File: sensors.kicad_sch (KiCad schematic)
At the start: 39 parts, among them J1 Amphenol_901-144, J2 Amphenol_901-144, Q1 BSS138DWQ-7, Q2 MBT2222ADW1T1, Q3 BSS138DWQ-7, Q4 MBT2222ADW1T1, Q5 MMDT2907, Q8 IRLML2803, Q9 NDS8434, U2 BMM150, U3 BMI270, U4 S1216V8, U5 EP2W+

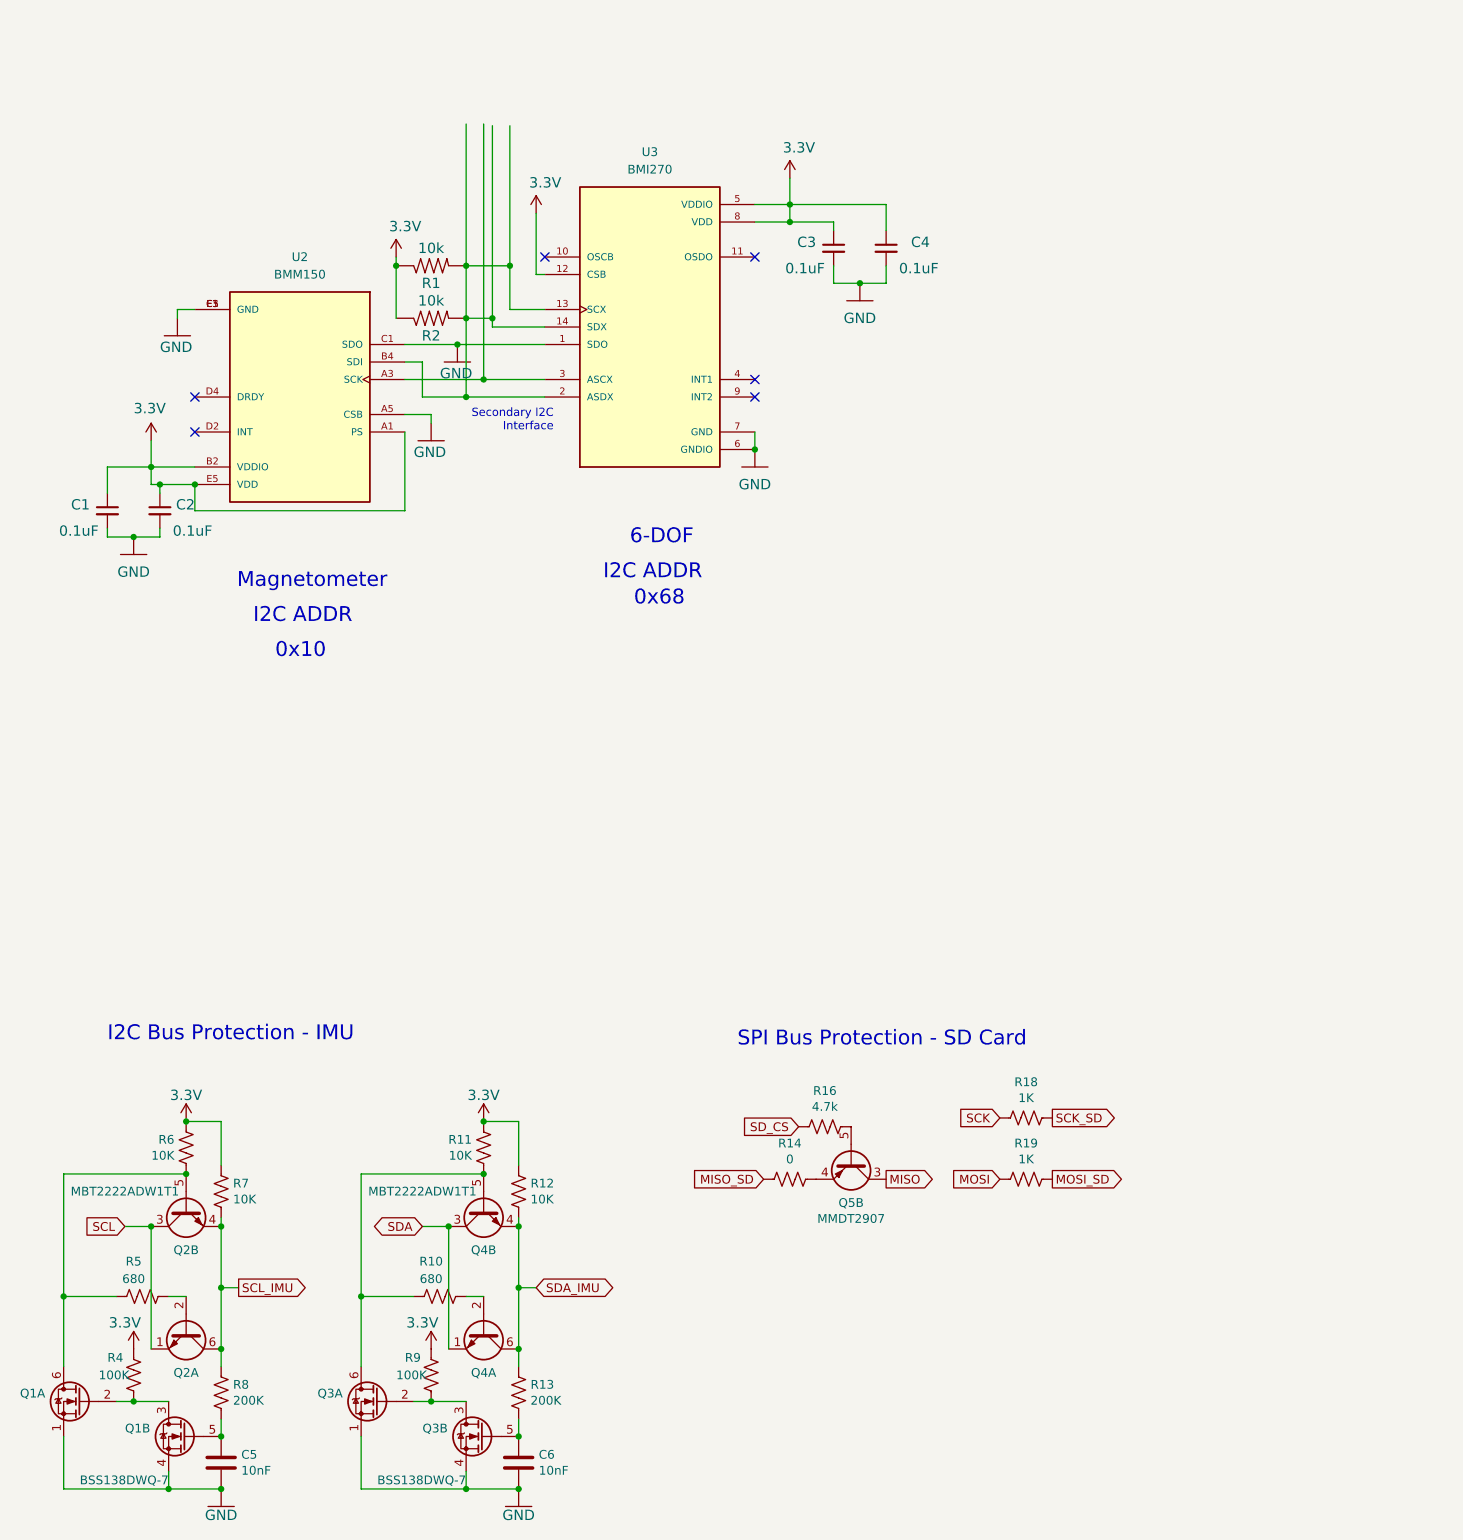
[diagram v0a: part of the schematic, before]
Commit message: update schematic
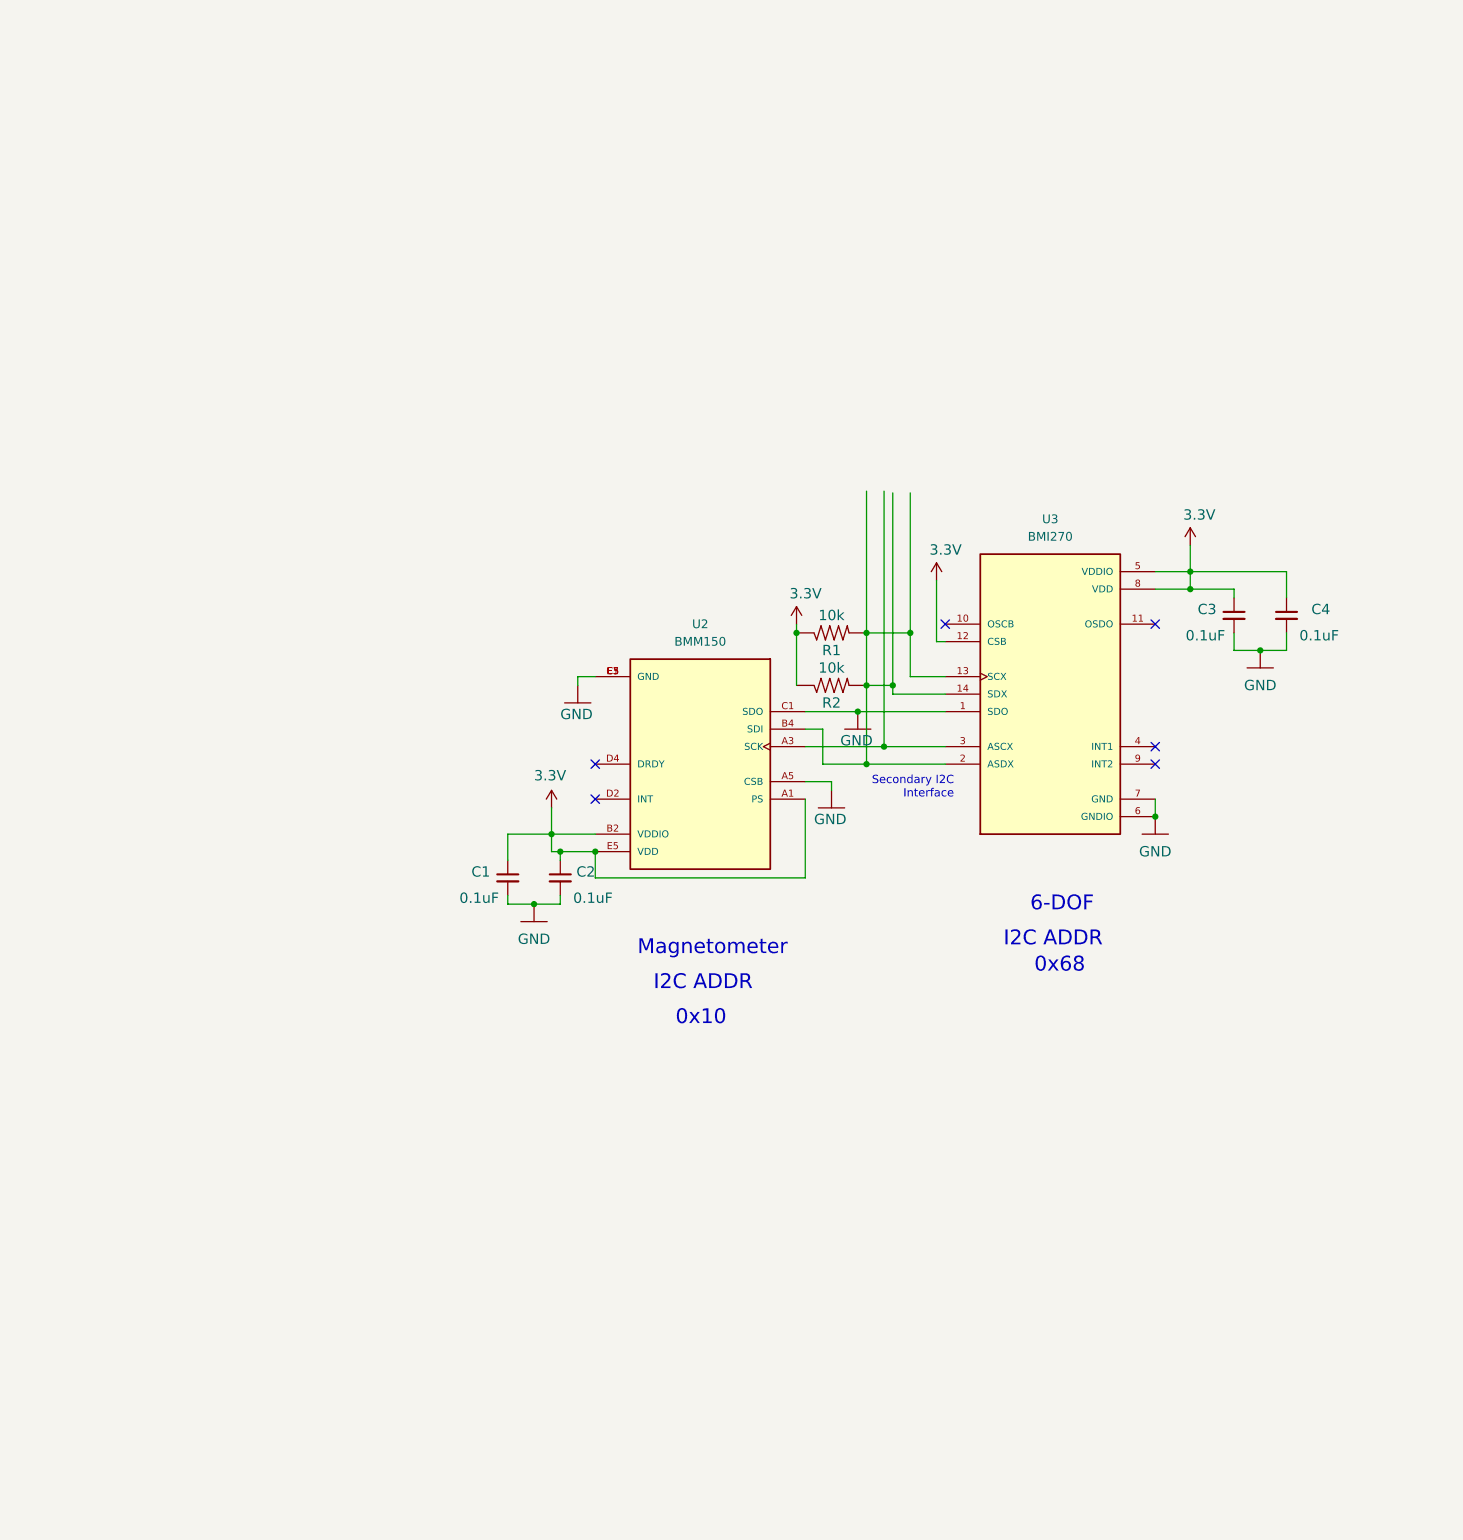
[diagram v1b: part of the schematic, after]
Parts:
- removed C5, C6: 10nF, Capacitor_SMD:C_0603_1608Metric, symbol Device:C
- removed Q1, Q3: BSS138DWQ-7, mainboard:BSS138DWQ-7, symbol mainboard:BSS138DWQ-7
- removed Q2, Q4: MBT2222ADW1T1, Package_TO_SOT_SMD:SOT-363_SC-70-6, symbol Transistor_BJT:MBT2222ADW1T1
- removed Q5: MMDT2907, Package_TO_SOT_SMD:SOT-363_SC-70-6, symbol mainboard:MMDT2907
- removed R10, R5: 680, Resistor_SMD:R_0603_1608Metric, symbol Device:R_US
- removed R11, R12, R6, R7: 10K, Resistor_SMD:R_0603_1608Metric, symbol Device:R_US
- removed R13, R8: 200K, Resistor_SMD:R_0603_1608Metric, symbol Device:R_US
- removed R14: 0, Resistor_SMD:R_0603_1608Metric, symbol Device:R_US
- removed R16: 4.7k, Resistor_SMD:R_0603_1608Metric, symbol Device:R_US
- removed R18, R19: 1K, Resistor_SMD:R_0603_1608Metric, symbol Device:R_US
- removed R4, R9: 100K, Resistor_SMD:R_0603_1608Metric, symbol Device:R_US
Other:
- note removed: "I2C Bus Protection - IMU"
- note removed: "SPI Bus Protection - SD Card"
- moved on the sheet: C1, C2, C3, C4, R1, R2, U2, U3

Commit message: hmm
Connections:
- net VBATT is gone; now on net GPS_PWR_IN: U4.22 (V_BCKP)
- net 3.3V: no longer Q9.1 (Source), Q9.2 (Source), Q9.3 (Source), R33.1
- net IMU_SCL: now reaches R1.2, R2.2, U2.B4 (SDI), U3.13 (SCX), U3.14 (SDX), U3.2 (ASDX)
- new net 3V3_IN: Q9.1 (Source), Q9.2 (Source), Q9.3 (Source), R33.1
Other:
- note added: "GPS_PWR_IN is 3v3 but from the PyCubed Mainboard regulator. This way, the GPS stays on when if the ADCS board resets (but not when the mainboard 3v3 regulator resets)."
- note added: "I originally made this circuit based on datasheet of the BMI270, and then handed off to evelyn. Nobody has tested the code with the secondary i2c interface, idk what the benefit of doing this would even be (other than just increasing available I2C address space). I don't think the address of the magnetometer is actuall 0x10"
- note added: "Per datasheet, V_BCKP current draw is 15 μA"
- note removed: "Per datasheet, V_BCKP current draw is 15 μA TODO do we want a seperate, always on 3v3 regulator here?"
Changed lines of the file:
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@@
   (junction (at 160.9852 108.1532) (diameter 0) (color 0 0 0 0)
-  )
-  (junction (at 157.1752 124.6632) (diameter 0) (color 0 0 0 0)
   )
   (junction (at 106.3752 147.5232) (diameter 0) (color 0 0 0 0)
@@
     (stroke (width 0) (type default))
   )
-  (wire (pts (xy 157.1752 124.6632) (xy 166.0652 124.6632))
+  (wire (pts (xy 145.7452 124.6632) (xy 166.0652 124.6632))
     (stroke (width 0) (type default))
   )
@@
     (stroke (width 0) (type default))
   )
-  (wire (pts (xy 157.1752 124.6632) (xy 157.1752 87.5792))
-    (stroke (width 0) (type default))
-  )
   (wire (pts (xy 158.4452 117.0432) (xy 158.4452 115.7732))
     (stroke (width 0) (type default))
   )
-  (wire (pts (xy 145.7452 124.6632) (xy 157.1752 124.6632))
-    (stroke (width 0) (type default))
-  )
   (wire (pts (xy 145.7452 129.7432) (xy 149.5552 129.7432))
     (stroke (width 0) (type default))
@@
     (stroke (width 0) (type default))
   )
-  (wire (pts (xy 158.4452 115.7732) (xy 158.4452 87.8332))
+  (wire (pts (xy 159.512 115.7732) (xy 159.512 84.0232))
     (stroke (width 0) (type default))
   )
@@
   )
   (wire (pts (xy 353.06 160.02) (xy 337.82 160.02))
+    (stroke (width 0) (type default))
+  )
+  (wire (pts (xy 159.512 115.7732) (xy 158.4452 115.7732))
     (stroke (width 0) (type default))
   )
@@
     (effects (font (size 2.159 2.159)) (justify left bottom))
   )
-  (text "Per datasheet, V_BCKP\ncurrent draw is 15 μA\n\nTODO do we want a\nseperate, always on \n3v3 regulator here?"
-    (at 356.87 88.9 0)
+  (text "Per datasheet, V_BCKP\ncurrent draw is 15 μA" (at 353.2632 88.9508 0)
     (effects (font (size 1.27 1.27)) (justify left bottom))
   )
-  (text "0x68" (at 186.3852 157.6832 0)
+  (text "I originally made this circuit based on datasheet of the BMI270, and \nthen handed off to evelyn. Nobody has tested the code with the secondary \ni2c interface, idk what the benefit of doing this would even be \n(other than just increasing available I2C address space).\n\nI don't think the address of the magnetometer is actuall 0x10\n"
+    (at 124.8664 182.4228 0)
+    (effects (font (size 1.2 1.2)) (justify left bottom))
+  )
+  (text "0x68" (at 185.0644 158.1404 0)
     (effects (font (size 2.159 2.159)) (justify right bottom))
   )
@@
     (effects (font (size 1.2 1.2)) (justify right bottom))
   )
-  (text "I2C ADDR" (at 188.9252 153.8732 0)
+  (text "I2C ADDR" (at 190.3984 153.8224 0)
     (effects (font (size 2.159 2.159)) (justify right bottom))
   )
@@
     (effects (font (size 2.159 2.159)) (justify right bottom))
   )
+  (text "GPS_PWR_IN is 3v3 but from the \nPyCubed Mainboard regulator. \nThis way, the GPS stays on when \nif the ADCS board resets (but not\nwhen the mainboard 3v3 regulator\nresets).\n"
+    (at 374.5484 103.4796 0)
+    (effects (font (size 1.27 1.27) (color 249 0 0 1)) (justify left bottom))
+  )
   (text "0x10\n" (at 134.3152 165.3032 0)
     (effects (font (size 2.159 2.159)) (justify right bottom))
@@
     (effects (font (size 1.27 1.27)) (justify left bottom))
   )
-  (global_label "GND" (shape bidirectional) (at 379.73 134.62 180) (fields_autoplaced)
-    (effects (font (size 0.254 0.254)) (justify right))
-    (property "Intersheetrefs" "${INTERSHEET_REFS}" (at 378.2988 134.62 0)
-      (effects (font (size 1.27 1.27)) (justify right) hide)
+  (global_label "IMU_SDA" (shape input) (at 159.512 84.0232 0) (fields_autoplaced)
+    (effects (font (size 1.27 1.27)) (justify left))
+    (property "Intersheetrefs" "${INTERSHEET_REFS}" (at 170.4196 84.0232 0)
+      (effects (font (size 1.27 1.27)) (justify left) hide)
     )
   )
@@
     )
   )
+  (global_label "3V3_IN" (shape bidirectional) (at 320.04 80.01 180) (fields_autoplaced)
+    (effects (font (size 1.27 1.27)) (justify right))
+    (property "Intersheetrefs" "${INTERSHEET_REFS}" (at 309.533 80.01 0)
+      (effects (font (size 1.27 1.27)) (justify right) hide)
+    )
+  )
   (global_label "GPS_PWR_IN" (shape bidirectional) (at 367.03 168.91 0) (fields_autoplaced)
     (effects (font (size 1.27 1.27)) (justify left))
@@
     )
   )
-  (global_label "GND" (shape bidirectional) (at 302.26 185.42 180) (fields_autoplaced)
-    (effects (font (size 0.254 0.254)) (justify right))
-    (property "Intersheetrefs" "${INTERSHEET_REFS}" (at 300.8288 185.42 0)
-      (effects (font (size 1.27 1.27)) (justify right) hide)
-    )
-  )
-  (global_label "VBATT" (shape bidirectional) (at 299.72 180.34 180) (fields_autoplaced)
-    (effects (font (size 1.27 1.27)) (justify right))
-    (property "Intersheetrefs" "${INTERSHEET_REFS}" (at 290.2411 180.34 0)
-      (effects (font (size 1.27 1.27)) (justify right) hide)
-    )
-  )
   (global_label "GPS_PWR_IN" (shape bidirectional) (at 351.79 92.71 0) (fields_autoplaced)
     (effects (font (size 1.27 1.27)) (justify left))
@@
     )
   )
-  (global_label "GND" (shape bidirectional) (at 337.82 154.94 180) (fields_autoplaced)
-    (effects (font (size 0.254 0.254)) (justify right))
-    (property "Intersheetrefs" "${INTERSHEET_REFS}" (at 336.3888 154.94 0)
-      (effects (font (size 1.27 1.27)) (justify right) hide)
-    )
-  )
   (global_label "RX_GPS" (shape bidirectional) (at 299.72 175.26 180) (fields_autoplaced)
     (effects (font (size 1.27 1.27)) (justify right))
@@
     )
   )
-  (global_label "GND" (shape bidirectional) (at 302.26 154.94 180) (fields_autoplaced)
-    (effects (font (size 0.254 0.254)) (justify right))
-    (property "Intersheetrefs" "${INTERSHEET_REFS}" (at 300.8288 154.94 0)
-      (effects (font (size 1.27 1.27)) (justify right) hide)
-    )
-  )
-  (global_label "GND" (shape bidirectional) (at 320.04 102.87 180) (fields_autoplaced)
-    (effects (font (size 0.254 0.254)) (justify right))
-    (property "Intersheetrefs" "${INTERSHEET_REFS}" (at 318.6088 102.87 0)
-      (effects (font (size 1.27 1.27)) (justify right) hide)
+  (global_label "GPS_PWR_IN" (shape bidirectional) (at 299.72 180.34 180) (fields_autoplaced)
+    (effects (font (size 1.27 1.27)) (justify right))
+    (property "Intersheetrefs" "${INTERSHEET_REFS}" (at 547.37 289.56 0)
+      (effects (font (size 1.27 1.27)) hide)
+    )
+  )
+  (global_label "IMU_SCL" (shape input) (at 160.9852 87.8332 0) (fields_autoplaced)
+    (effects (font (size 1.27 1.27)) (justify left))
+    (property "Intersheetrefs" "${INTERSHEET_REFS}" (at 171.8323 87.8332 0)
+      (effects (font (size 1.27 1.27)) (justify left) hide)
     )
   )
@@
         )
       )
-    )
-  )
-  (symbol (lib_id "mainboard:3.3V") (at 320.04 80.01 0) (unit 1)
-    (in_bom yes) (on_board yes) (dnp no)
-    (property "Reference" "#SUPPLY06" (at 320.04 80.01 0)
-      (effects (font (size 1.27 1.27)) hide)
-    )
-    (property "Value" "3.3V" (at 320.04 74.93 0)
-      (effects (font (size 1.4986 1.4986)))
-    )
-    (property "Footprint" "" (at 320.04 80.01 0)
-      (effects (font (size 1.27 1.27)) hide)
-    )
-    (property "Datasheet" "" (at 320.04 80.01 0)
-      (effects (font (size 1.27 1.27)) hide)
-    )
-    (pin "1")
-    (instances
-      (project "adcs-hardware"
-        (path "/2bf29f96-8e90-4c56-8856-49bc3b5fab50/c57143de-a118-4c83-b882-63fc675c961e"
-          (reference "#SUPPLY06") (unit 1)
-        )
-      )
-      (project "mainboard"
-        (path "/db20b18b-d25a-428e-8229-70a189e1de75/00000000-0000-0000-0000-00005cec5dde"
-          (reference "#SUPPLY06") (unit 1)
-        )
-      )

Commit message: organize
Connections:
- net 3.3V: no longer U2.A1 (PS)
- net RX_GPS: now also U4.21 (RXD); no longer U4.20 (TXD)
- net TX_GPS: now also U4.20 (TXD); no longer U4.21 (RXD)
- net at U3.3 (ASCX): no longer U2.A3 (SCK)
- net 3V3_IN renamed +3V3
- net +3V3: now also U2.A1 (PS)
- net GPS_PWR_IN renamed 3V3_GPS
- net IMU_SCL renamed SDA_IMU
- net SDA_IMU: no longer R1.2, U3.13 (SCX), U3.2 (ASDX)
- new net SCL_IMU: R1.2, U2.A3 (SCK), U3.13 (SCX)
- no-connect marks 20 -> 22
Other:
- note added: "6DOF SDO: bit 0 | SDO | ADDR | |-----|------| | GND | 0x68 | | 3V3 | 0x69 |"
- note added: "Magnetometer CSB: bit 0 SDO: bit 1 00100 | CSB | SDO | ADDR | |-----|-----|------| | GND | GND | 0x10 |"
- note removed: "0x10"
- note removed: "0x68"
- note removed: "6-DOF"
- note removed: "GPS_PWR_IN is 3v3 but from the PyCubed Mainboard regulator. This way, the GPS stays on when if the ADCS board resets (but not when the mainboard 3v3 regulator resets)."
- note removed: "I originally made this circuit based on datasheet of the BMI270, and then handed off to evelyn. Nobody has tested the code with the secondary i2c interface, idk what the benefit of doing this would even be (other than just increasing available I2C address space). I don't think the address of the magnetometer is actuall 0x10"
- note removed: "I2C ADDR"
- note removed: "Magnetometer"
- note removed: "Secondary I2C Interface"
- moved on the sheet: C1, C2, C3, C4, J1, J2, Q8, Q9, R1, R2, R3, R31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

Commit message: ready for review
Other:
- moved on the sheet: C1, C2, C3, C4, J1, J2, Q8, Q9, R1, R2, R3, R31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

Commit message: pete feedback
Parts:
- added C32: 10nF, symbol pycubed_mainboard:10NF_10000PF-50V-10%(0603)
- added C50: 10uF, symbol pycubed_mainboard:10NF_10000PF-50V-10%(0603)
- added C51: 4.7uF, symbol pycubed_mainboard:10NF_10000PF-50V-10%(0603)
- added C52: 0.22uF, symbol pycubed_mainboard:10NF_10000PF-50V-10%(0603)
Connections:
- net 3V3_GPS: now also C32.1, C50.1, C51.1, C52.1
- net ENAB_GPS renamed EN_GPS
- new net: C32.2, C50.2, C51.2, C52.2
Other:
- note added: "Consider using the secondary I2C interface on the BMI270 Pros: - coherent data Cons: - if one device fails, they both fail? Or could we put isolation circuitry on the secondary interface?"
- note added: "Per Orion B16 datasheet, V_BCKP current draw is 15 μA"
- note removed: "Per datasheet, V_BCKP current draw is 15 μA"
- moved on the sheet: J1, J2, Q8, Q9, R3, R31, R32, R33, U4, U5
